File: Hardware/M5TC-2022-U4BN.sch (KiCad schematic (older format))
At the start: 68 parts, among them J1 VCC, J10 SLIDE_DATA_0, J11 SLIDE_DATA_1, J12 SLIDE_DATA_2, J13 SLIDE_DATA_3, J14 ISP, J15 A-G, J2 GND, J3 DATA_0, J4 DATA_1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

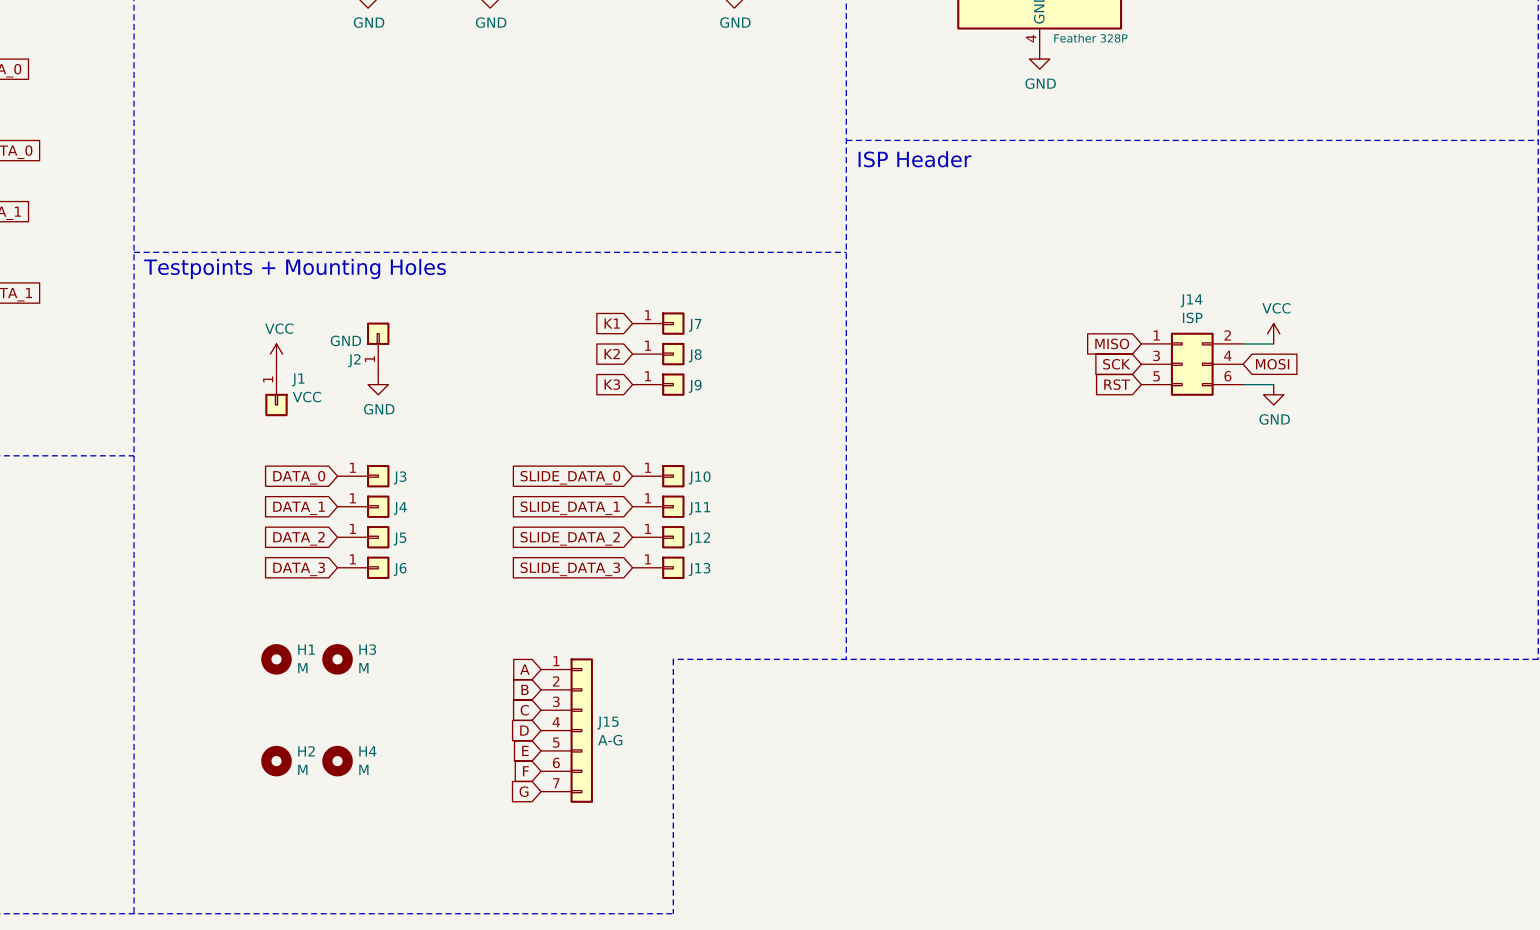
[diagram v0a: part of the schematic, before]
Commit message: Added triple test points
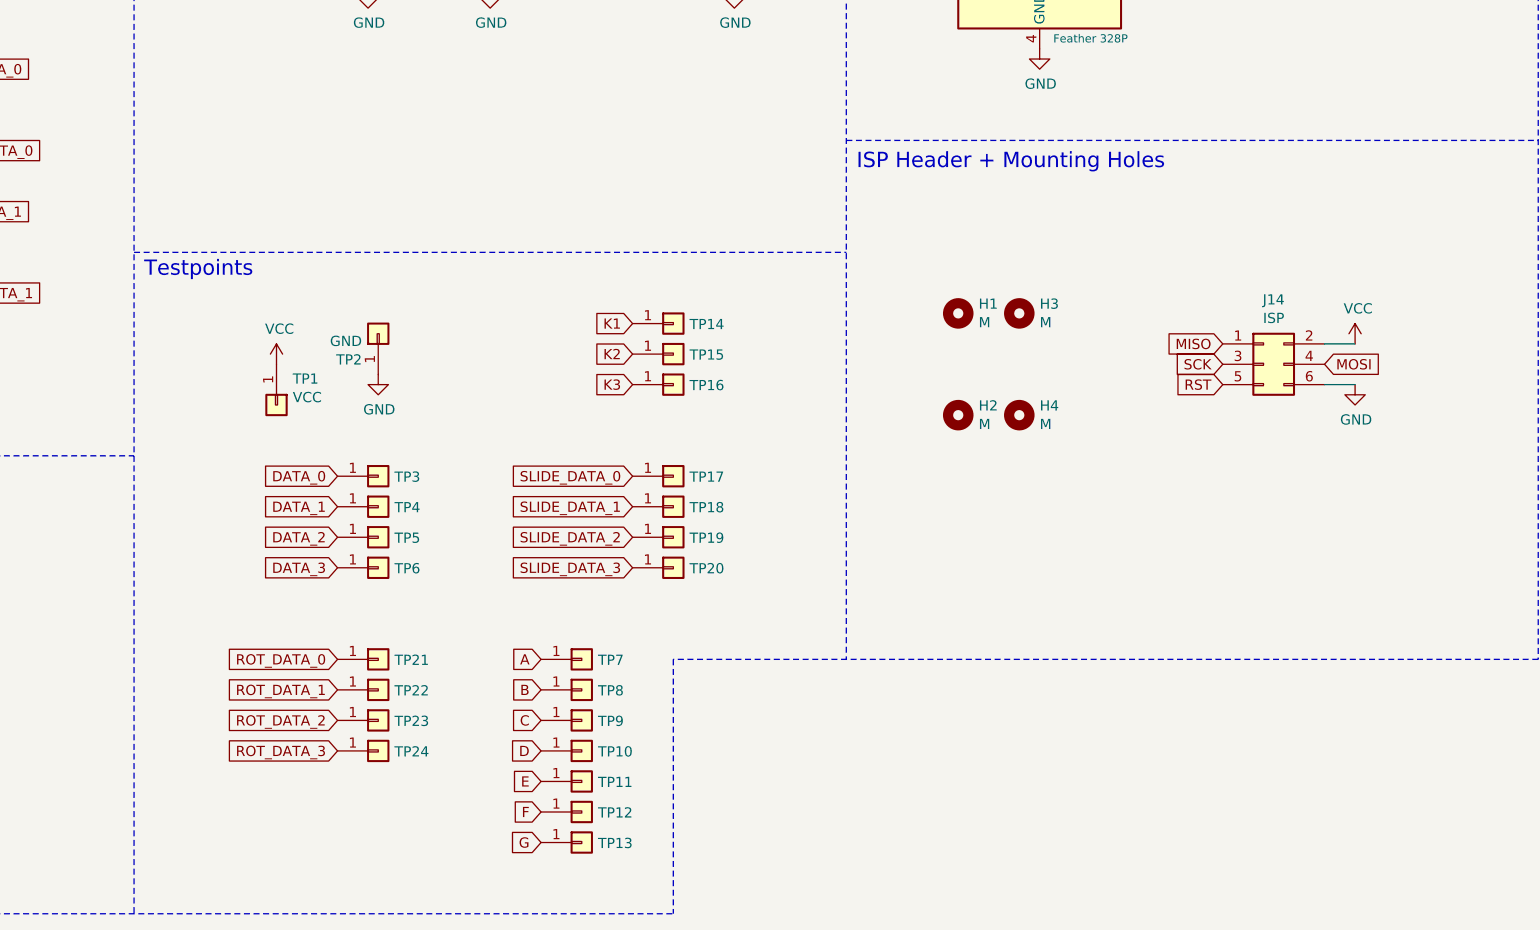
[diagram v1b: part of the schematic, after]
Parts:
- removed J15: A-G, Connector_PinSocket_2.54mm:PinSocket_1x07_P2.54mm_Vertical, symbol Connector_Generic:Conn_01x07
- added TP10, TP11, TP12, TP13, TP7, TP8, TP9: Conn_01x01, Custom_TestPoint:TestPoint_LoopPost, symbol Connector_Generic:Conn_01x01
- added TP21: ROT_DATA_0, Custom_TestPoint:TestPoint_LoopPostPad, symbol Connector_Generic:Conn_01x01
- added TP22: ROT_DATA_1, Custom_TestPoint:TestPoint_LoopPostPad, symbol Connector_Generic:Conn_01x01
- added TP23: ROT_DATA_2, Custom_TestPoint:TestPoint_LoopPostPad, symbol Connector_Generic:Conn_01x01
- added TP24: ROT_DATA_3, Custom_TestPoint:TestPoint_LoopPostPad, symbol Connector_Generic:Conn_01x01
- TP1: renamed from J1; footprint TestPoint:TestPoint_Loop_D3.80mm_Drill2.0mm -> Custom_TestPoint:TestPoint_LoopPostPad
- TP14: renamed from J7; footprint TestPoint:TestPoint_Loop_D2.50mm_Drill1.0mm -> Custom_TestPoint:TestPoint_LoopPostPad
- TP15: renamed from J8; footprint TestPoint:TestPoint_Loop_D2.50mm_Drill1.0mm -> Custom_TestPoint:TestPoint_LoopPostPad
- TP16: renamed from J9; footprint TestPoint:TestPoint_Loop_D2.50mm_Drill1.0mm -> Custom_TestPoint:TestPoint_LoopPostPad
- TP17: renamed from J10; footprint TestPoint:TestPoint_Loop_D2.50mm_Drill1.0mm -> Custom_TestPoint:TestPoint_LoopPostPad
- TP18: renamed from J11; footprint TestPoint:TestPoint_Loop_D2.50mm_Drill1.0mm -> Custom_TestPoint:TestPoint_LoopPostPad
- TP19: renamed from J12; footprint TestPoint:TestPoint_Loop_D2.50mm_Drill1.0mm -> Custom_TestPoint:TestPoint_LoopPostPad
- TP2: renamed from J2; footprint TestPoint:TestPoint_Loop_D3.80mm_Drill2.0mm -> Custom_TestPoint:TestPoint_LoopPostPad
- TP20: renamed from J13; footprint TestPoint:TestPoint_Loop_D2.50mm_Drill1.0mm -> Custom_TestPoint:TestPoint_LoopPostPad
- TP3: renamed from J3; footprint TestPoint:TestPoint_Loop_D2.50mm_Drill1.0mm -> Custom_TestPoint:TestPoint_LoopPostPad
- TP4: renamed from J4; footprint TestPoint:TestPoint_Loop_D2.50mm_Drill1.0mm -> Custom_TestPoint:TestPoint_LoopPostPad
- TP5: renamed from J5; footprint TestPoint:TestPoint_Loop_D2.50mm_Drill1.0mm -> Custom_TestPoint:TestPoint_LoopPostPad
- TP6: renamed from J6; footprint TestPoint:TestPoint_Loop_D2.50mm_Drill1.0mm -> Custom_TestPoint:TestPoint_LoopPostPad
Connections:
- net A: now also TP7.1 (Pin_1)
- net B: now also TP8.1 (Pin_1)
- net C: now also TP9.1 (Pin_1)
- net D: now also TP10.1 (Pin_1)
- net E: now also TP11.1 (Pin_1)
- net F: now also TP12.1 (Pin_1)
- net G: now also TP13.1 (Pin_1)
- net ROT_DATA_0: now also TP21.1 (Pin_1)
- net ROT_DATA_1: now also TP22.1 (Pin_1)
- net ROT_DATA_2: now also TP23.1 (Pin_1)
- net ROT_DATA_3: now also TP24.1 (Pin_1)
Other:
- note added: "ISP Header + Mounting Holes"
- note added: "Testpoints\n\n"
- note removed: "ISP Header"
- note removed: "Testpoints + Mounting Holes\n\n"
- moved on the sheet: H1, H2, H3, H4, J14

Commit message: Rerouted Board, Changed SOIC-Hex Size
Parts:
- SW1, SW2, SW3, SW4: footprint SparkFun-Electromechanical:SWITCH-SPDT -> 4PDT_Footprint:E-Switch-EG1218
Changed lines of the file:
@@
 F 0 "SW1" V 1850 1550 50  0000 R CNN
 F 1 "SW_SPDT" V 1505 1312 50  0001 R CNN
-F 2 "SparkFun-Electromechanical:SWITCH-SPDT" H 1550 1500 50  0001 C CNN
+F 2 "4PDT_Footprint:E-Switch-EG1218" H 1550 1500 50  0001 C CNN
 F 3 "~" H 1550 1500 50  0001 C CNN
 	1    1550 1500
@@
 F 0 "SW2" V 2250 1550 50  0000 R CNN
 F 1 "SW_SPDT" V 1905 1312 50  0001 R CNN
-F 2 "SparkFun-Electromechanical:SWITCH-SPDT" H 1950 1500 50  0001 C CNN
+F 2 "4PDT_Footprint:E-Switch-EG1218" H 1950 1500 50  0001 C CNN
 F 3 "~" H 1950 1500 50  0001 C CNN
 	1    1950 1500
@@
 F 0 "SW3" V 2650 1550 50  0000 R CNN
 F 1 "SW_SPDT" V 2305 1312 50  0001 R CNN
-F 2 "SparkFun-Electromechanical:SWITCH-SPDT" H 2350 1500 50  0001 C CNN
+F 2 "4PDT_Footprint:E-Switch-EG1218" H 2350 1500 50  0001 C CNN
 F 3 "~" H 2350 1500 50  0001 C CNN
 	1    2350 1500
@@
 F 0 "SW4" V 3050 1550 50  0000 R CNN
 F 1 "SW_SPDT" V 2705 1312 50  0001 R CNN
-F 2 "SparkFun-Electromechanical:SWITCH-SPDT" H 2750 1500 50  0001 C CNN
+F 2 "4PDT_Footprint:E-Switch-EG1218" H 2750 1500 50  0001 C CNN
 F 3 "~" H 2750 1500 50  0001 C CNN
 	1    2750 1500
